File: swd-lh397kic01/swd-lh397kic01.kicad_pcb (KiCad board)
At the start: 4 copper layers, 28.8 x 25.2 mm, 18 parts, among them J1 1-1734248-5, J2 10051922-2010ELF, SW1 SMD-BUTTON_4P-5.2X5.2X1.5MM-S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, U1 RS3236-2.5FY5, U3 AP3127B

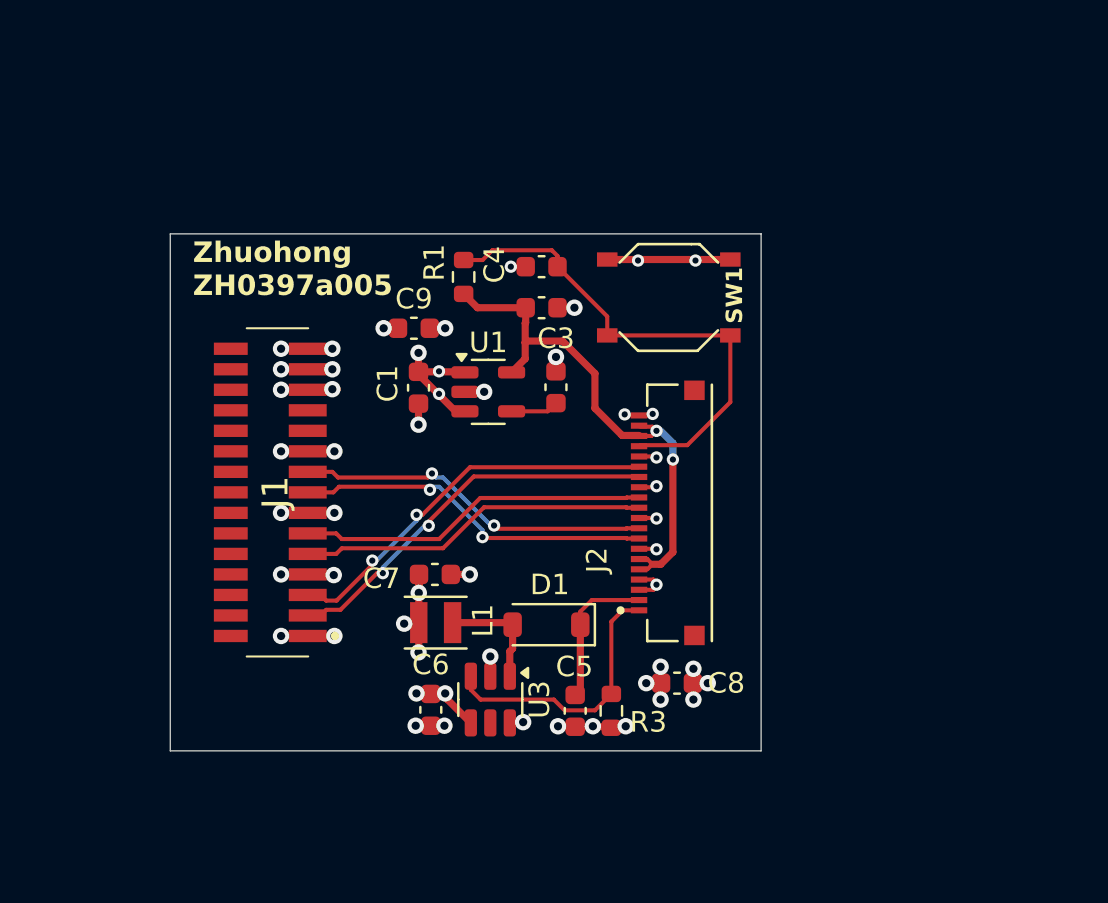
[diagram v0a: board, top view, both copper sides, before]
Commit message: Add LCSC numbers to C's and R's
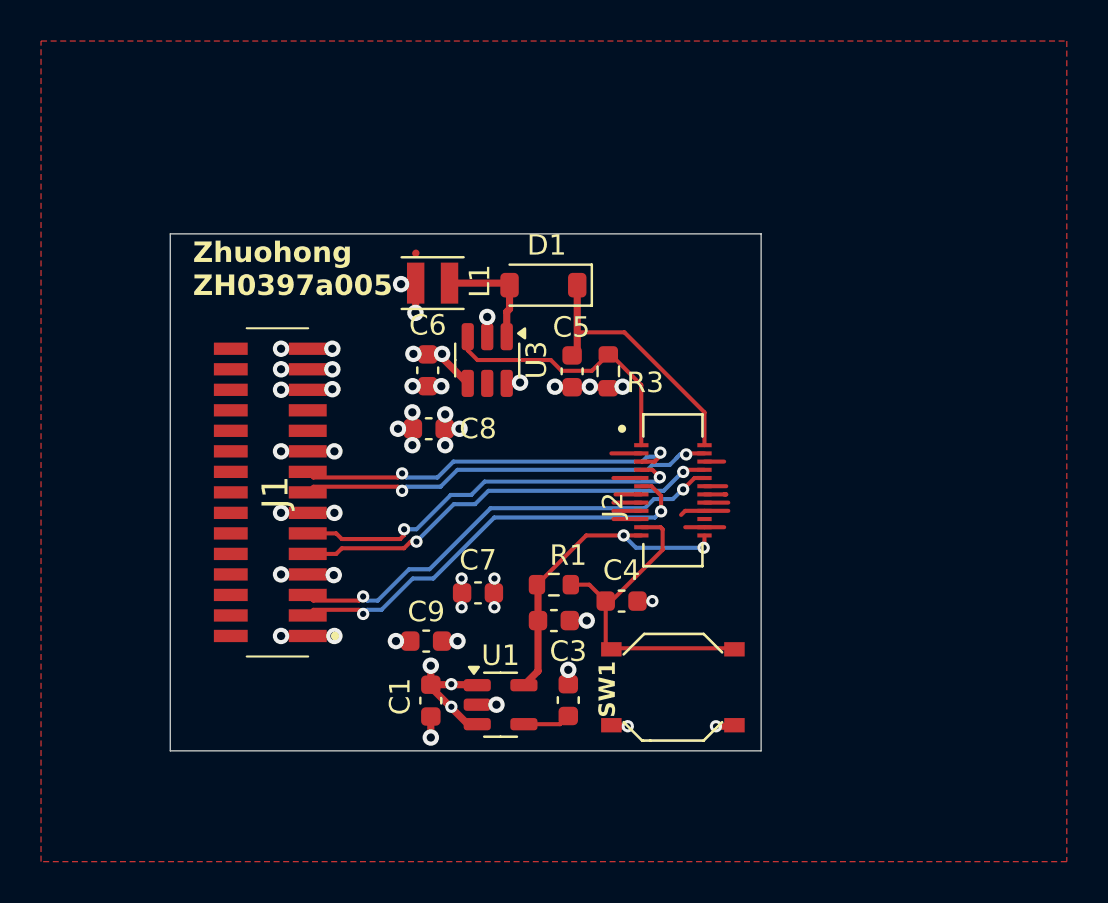
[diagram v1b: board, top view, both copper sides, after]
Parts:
- J2: value 10051922-2010ELF -> DF40C-24DS-0.4V_51_; footprint custom:AMPHENOL_10051922-2010ELF -> custom:HIROSE_DF40C-24DS-0.4V_51_
- moved SW1 19.0 mm to (90.8, 71.5), turned to 0 degrees
- moved C8 17.3 mm to (78.9, 58.9)
- moved C4 16.8 mm to (88.3, 67.3), turned to 0 degrees
- moved C5 16.6 mm to (85.9, 56.1)
- moved D1 16.6 mm to (84.5, 51.9)
- moved R3 16.6 mm to (87.7, 56.1)
- moved C6 16.6 mm to (78.8, 56.0)
- moved L1 16.6 mm to (79.1, 51.8)
- moved U3 16.6 mm to (81.8, 55.5)
- moved R1 15.6 mm to (85.0, 66.5), turned to 0 degrees
- moved C1 15.3 mm to (79.0, 72.2)
- moved C2 15.3 mm to (85.0, 68.2)
- moved C3 15.3 mm to (85.7, 72.1)
- moved C9 15.3 mm to (78.8, 69.2)
- moved U1 15.3 mm to (82.4, 72.3)
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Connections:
- J2 pad 10: GND -> D1_P
- J2 pad 11: CLK_C_N -> D1_N
- J2 pad 12: CLK_C_P -> GND
- J2 pad 14: D1_N -> GND
- J2 pad 15: D1_P -> GND
- J2 pad 17: RST -> GND
- J2 pad 18: +2V8 -> GND
- J2 pad 19: +2V8 -> GND
- J2 pad 20: GND -> TE
- J2 pad 4: GND -> D0_N
- J2 pad 5: +2V8 -> D0_P
- J2 pad 6: +2V8 -> GND
- J2 pad 7: GND -> CLK_C_P
- J2 pad 8: D0_N -> CLK_C_N
- J2 pad 9: D0_P -> GND
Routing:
- net +2V8: track 26.0 -> 16.0 mm
- net RST: track 24.3 -> 16.7 mm
- net GND: track 40.1 -> 46.1 mm, vias 35 -> 29
- net LEDA: track 6.91 -> 12.6 mm
- net CLK_C_N: track 17.1 -> 21.0 mm, vias 0 -> 2
- net D1_P: track 18.6 -> 22.1 mm
- net D1_N: track 18.6 -> 21.4 mm
- net CLK_C_P: track 17.1 -> 19.8 mm, vias 0 -> 2
- net D0_N: track 17.6 -> 20.3 mm
- net +3V3: track 23.4 -> 21.7 mm, vias 17 -> 18
- net D0_P: track 17.5 -> 19.2 mm
- added copper zone on F.Cu, net GND

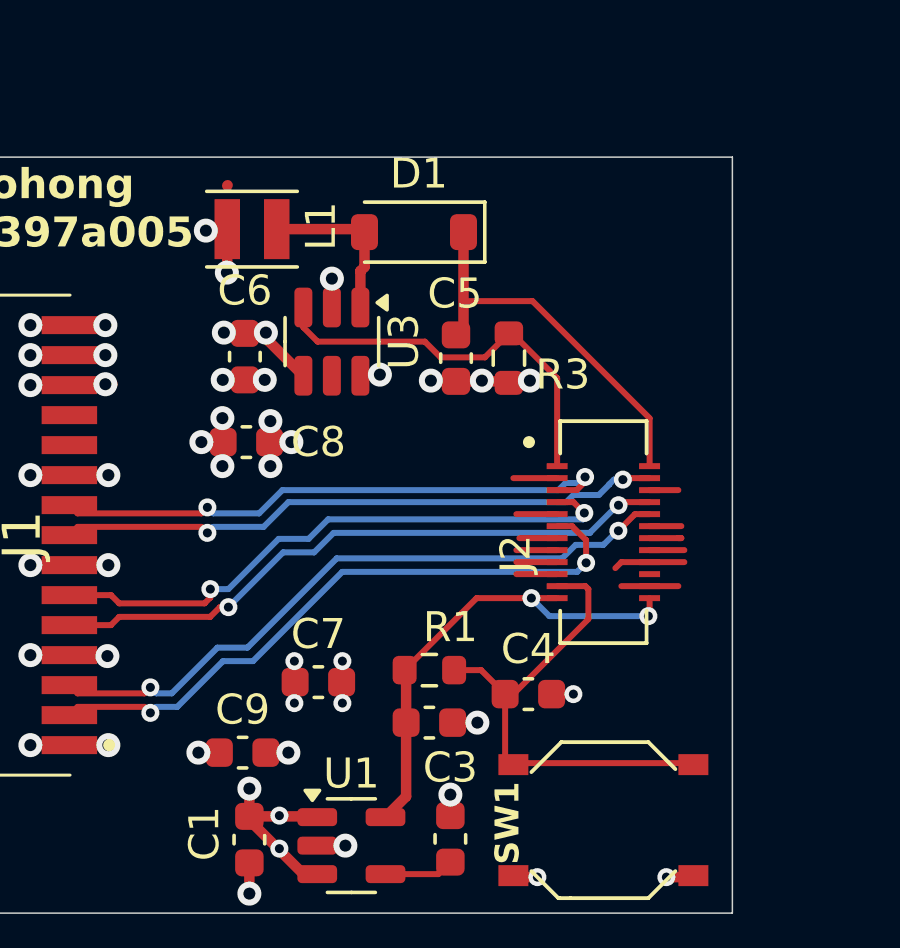
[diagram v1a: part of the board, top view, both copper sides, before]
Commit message: Fix names, footprints, and silkscreen of the pcb's
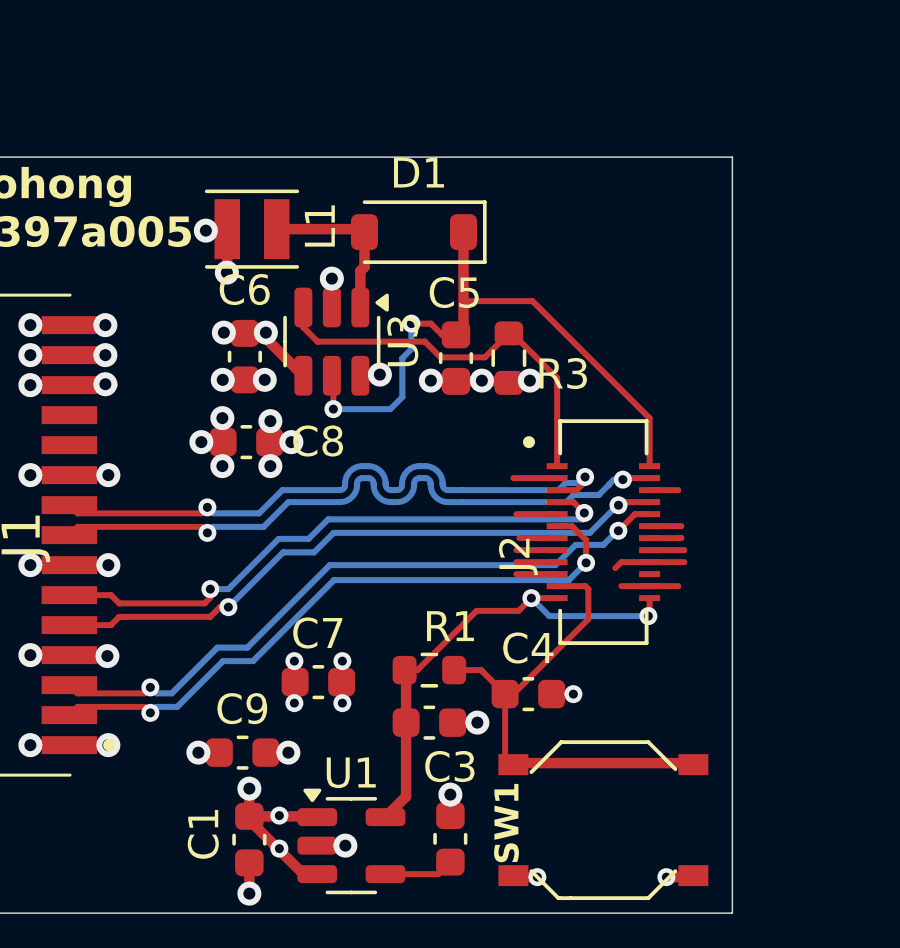
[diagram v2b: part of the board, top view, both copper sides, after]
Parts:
- R3: value 6R2 1% -> 14R7 0.1%
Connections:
- U3 pad 5: (no net) -> LEDA
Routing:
- net LEDA: track 12.6 -> 20.4 mm, vias 0 -> 2
- net D0_P: track 19.2 -> 21.0 mm
- net D0_N: track 20.3 -> 22.1 mm

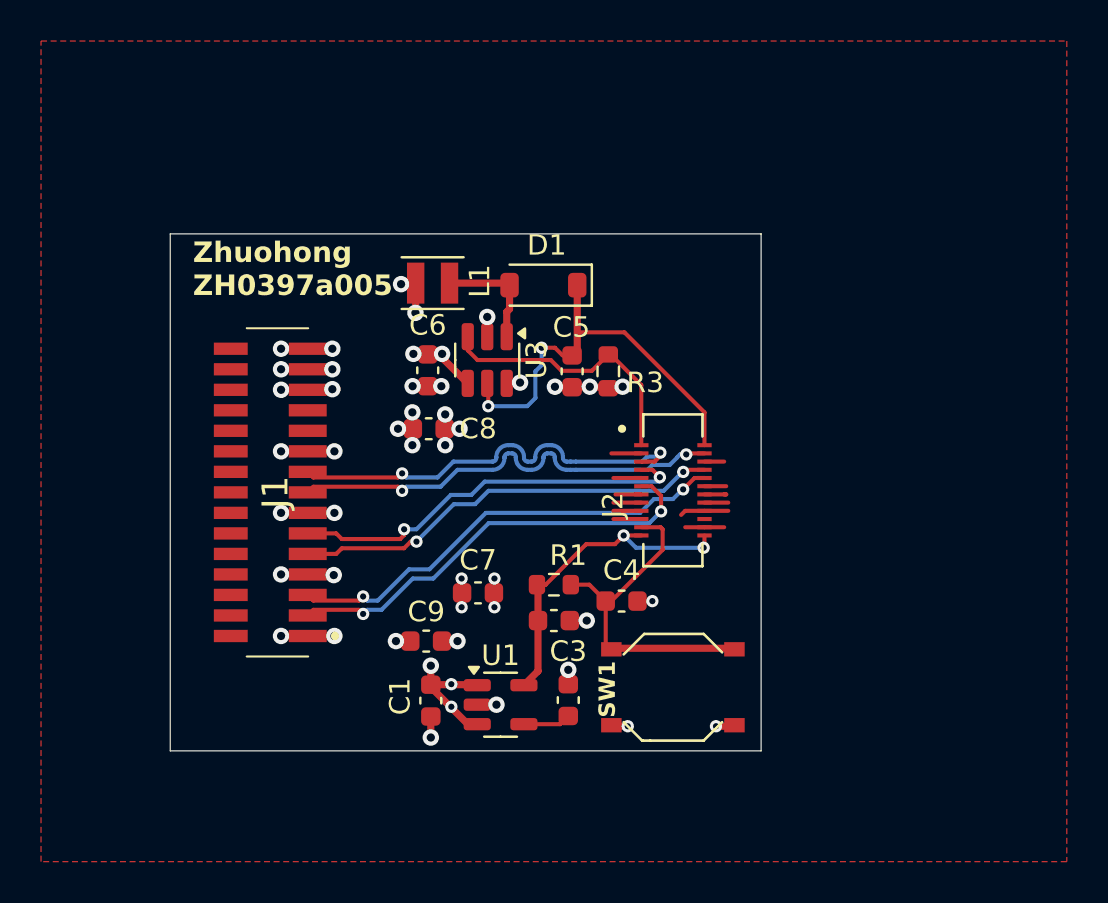
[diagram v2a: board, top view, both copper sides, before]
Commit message: Add LCSC labels that were missing for swd lh397kic01
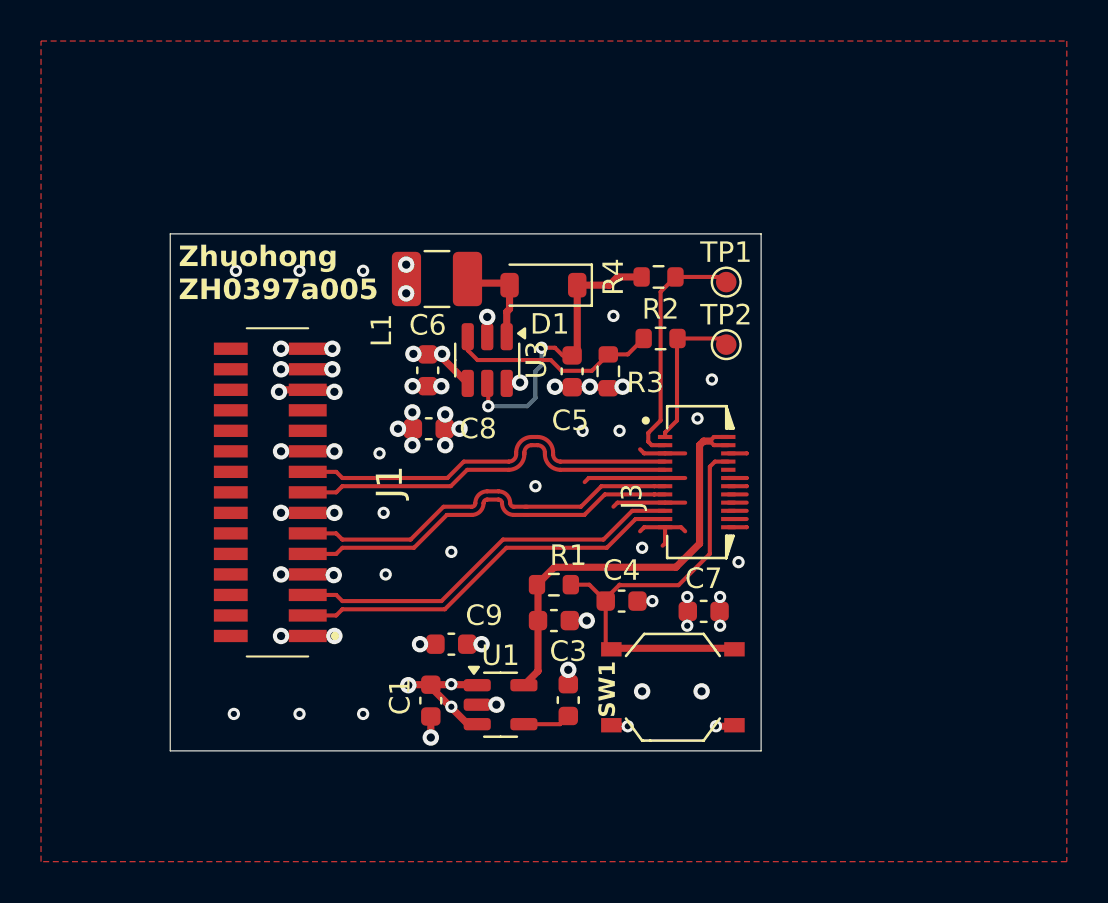
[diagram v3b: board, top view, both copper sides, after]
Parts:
- removed J2: DF40C-24DS-0.4V_51_, custom:HIROSE_DF40C-24DS-0.4V_51_
- added J3: LH397K, custom:LH397K-IC01, F.Cu at (92.0, 61.5)
- added R2: 0, Resistor_SMD:R_0603_1608Metric, F.Cu at (90.2, 54.5)
- added R4: 0, Resistor_SMD:R_0603_1608Metric, F.Cu at (90.1, 51.5)
- added TP1: TestPoint, TestPoint:TestPoint_Pad_D1.0mm, F.Cu at (93.4, 51.8)
- added TP2: TestPoint, TestPoint:TestPoint_Pad_D1.0mm, F.Cu at (93.4, 54.8)
- L1: value 22uH -> 6.8uH; footprint Inductor_SMD:L_Changjiang_FNR252010S -> Inductor_SMD:L_1210_3225Metric_Pad1.42x2.65mm_HandSolder
- R3: value 14R7 0.1% -> 10R0 1%
- U3: value AP3127B -> AP3032B
- moved C7 11.0 mm to (92.3, 67.8)
- moved C9 1.23 mm to (80.0, 69.4), turned to 180 degrees
- moved L1 0.29 mm to (79.3, 51.6)
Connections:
- net LEDA renamed Net-(D1-K)
- net LEDK renamed Net-(U3-FB)
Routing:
- net LEDA: track 0.00 -> 11.7 mm
- net LEDK: track 0.00 -> 7.51 mm
- net Net-(D1-K): track 20.4 -> 14.2 mm
- net RST: track 16.7 -> 22.1 mm
- net +2V8: track 16.0 -> 21.3 mm, vias 2 -> 0
- net GND: track 46.1 -> 50.7 mm, vias 29 -> 49
- net Net-(U3-FB): track 13.4 -> 10.3 mm
- net D0_N: track 22.1 -> 19.2 mm, vias 2 -> 0
- net D1_P: track 22.1 -> 19.4 mm, vias 2 -> 0
- net +3V3: track 21.6 -> 19.4 mm
- net D1_N: track 21.4 -> 19.4 mm, vias 2 -> 0
- net D0_P: track 21.0 -> 19.2 mm, vias 2 -> 0
- net CLK_C_N: track 21.0 -> 19.4 mm, vias 2 -> 0
- net Net-(D1-A): track 5.39 -> 4.32 mm
- net CLK_C_P: track 19.8 -> 19.4 mm, vias 2 -> 0

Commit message: Fix parts for board LMT040WM004C
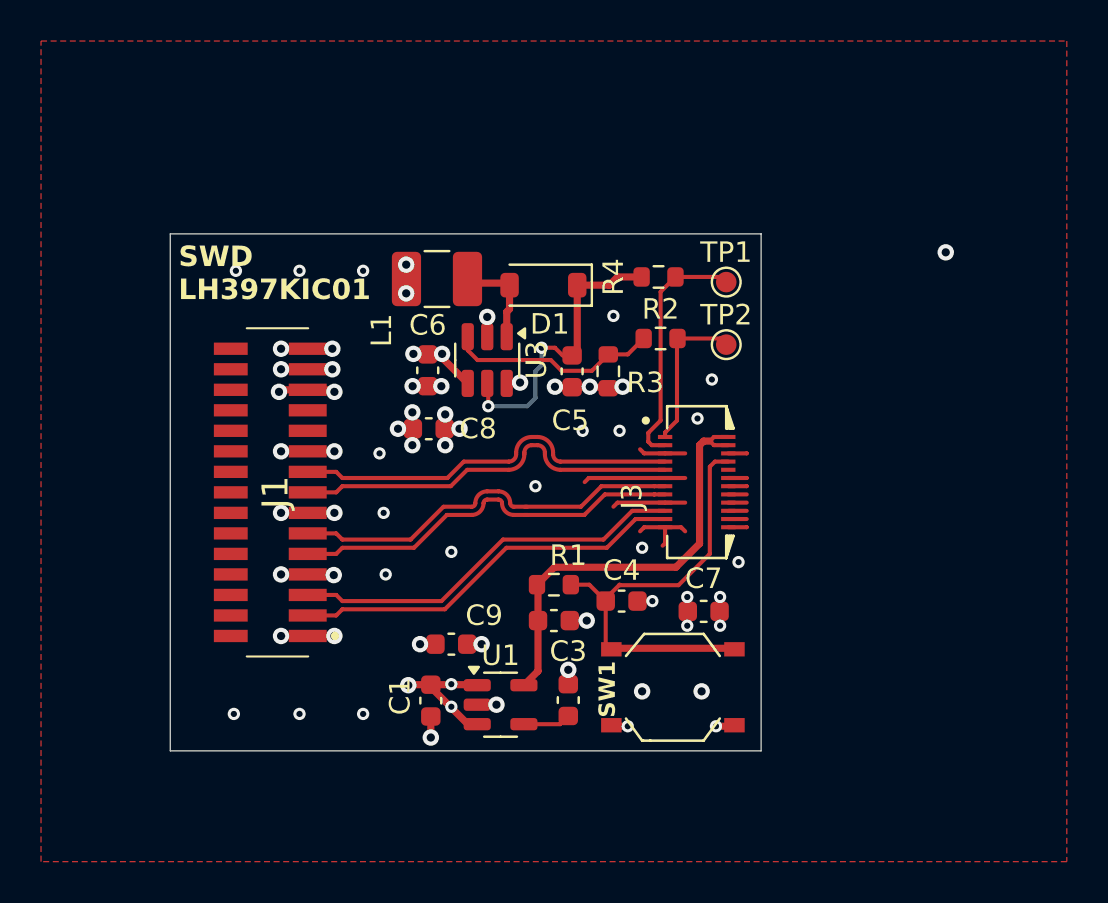
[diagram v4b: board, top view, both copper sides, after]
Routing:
- net (no net): vias 0 -> 1
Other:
- board text added: "SWD LH397KIC01"
- board text removed: "Zhuohong ZH0397a005"
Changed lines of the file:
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@@
 		)
 		(pad_to_mask_clearance 0)
-		(solder_mask_min_width 0.1016)
 		(allow_soldermask_bridges_in_footprints no)
 		(pcbplotparams
@@
 			(plot_on_all_layers_selection 0x0000000_00000000)
 			(disableapertmacros no)
-			(usegerberextensions no)
+			(usegerberextensions yes)
 			(usegerberattributes yes)
 			(usegerberadvancedattributes yes)
@@
 			(plotinvisibletext no)
 			(sketchpadsonfab no)
-			(subtractmaskfromsilk no)
+			(subtractmaskfromsilk yes)
 			(outputformat 1)
 			(mirror no)
-			(drillshape 1)
+			(drillshape 0)
 			(scaleselection 1)
-			(outputdirectory "")
+			(outputdirectory "plots/")
 		)
 	)
@@
 			)
 		)
-		(property "LCSC" " C7497031"
+		(property "LCSC" "  C394999"
 			(at 0 0 0)
 			(unlocked yes)
@@
 			)
 		)
-		(property "LCSC" "C5189821"
+		(property "LCSC" "C386149"
 			(at 0 0 90)
 			(unlocked yes)
@@
 			)
 		)
-		(property "LCSC" "C5189821"
+		(property "LCSC" "C386149"
 			(at 0 0 -90)
 			(unlocked yes)
@@
 			)
 		)
-		(property "LCSC" "C5189821"
+		(property "LCSC" "C386149"
 			(at 0 0 -90)
 			(unlocked yes)
@@
 		(tags "Connector")
 		(property "Reference" "J1"
-			(at -0.5 -3.975 -90)
+			(at 0 1.6 -90)
 			(layer "F.SilkS")
 			(effects
@@
 			)
 		)
-		(property "LCSC" "C5189821"
+		(property "LCSC" "C386149"
 			(at 0 0 0)
 			(unlocked yes)
@@
 			)
 		)
+		(property "LCSC" "C424640"
+			(at 0 0 0)
+			(unlocked yes)
+			(layer "F.Fab")
+			(hide yes)
+			(effects
+				(font
+					(size 1 1)
+					(thickness 0.15)
+				)
+			)
+		)
 		(sheetname "MIPI DSI OUT")
 		(sheetfile "mipi-dsi-out.kicad_sch")
@@
 			)
 		)
-		(property "Lcsc" "C379345"
+		(property "LCSC" "C379345"
 			(at 0 0 0)
 			(unlocked yes)
@@
 			)
 		)
-		(property "LCSC" "C2114035"
+		(property "LCSC" " C103222"
 			(at 0 0 -90)
 			(unlocked yes)
@@
 			)
 		)
-		(property "LCSC" "C2766941"
+		(property "LCSC" "C3016185"
 			(at 0 0 0)
 			(unlocked yes)
@@
 			)
 		)
-		(property "LCSC" "C5189821"
+		(property "LCSC" "C386149"
 			(at 0 0 0)
 			(unlocked yes)
@@
 		(sheetname "VOLTAGE REGULATORS")
 		(sheetfile "voltage-regulators.kicad_sch")
-		(attr exclude_from_pos_files)
+		(attr exclude_from_pos_files dnp)
 		(fp_circle
 			(center 0 0)
@@
 			)
 		)
-		(property "LCSC" "C2766941"
+		(property "LCSC" "C3016185"
 			(at 0 0 0)
 			(unlocked yes)
@@
 		(sheetname "VOLTAGE REGULATORS")
 		(sheetfile "voltage-regulators.kicad_sch")
-		(attr exclude_from_pos_files)
+		(attr exclude_from_pos_files dnp)
 		(fp_circle
 			(center 0 0)
@@
 		(layer "Edge.Cuts")
 	)
-	(gr_text "Zhuohong\nZH0397a005"
+	(gr_text "SWD\nLH397KIC01"
 		(at 66.7 52.7 0)
 		(layer "F.SilkS")
@@
 			(extension_offset 0.5) keep_text_aligned)
 	)
+	(via
+		(at 104.1 50.3)
+		(size 0.8)
+		(drill 0.4)
+		(layers "F.Cu" "B.Cu")
+		(net 0)
+	)
 	(segment
